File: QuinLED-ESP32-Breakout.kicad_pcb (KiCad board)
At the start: 2 copper layers, 60.8 x 83.7 mm, 22 parts, among them Q1 BC547, U1 QuinLED-ESP32

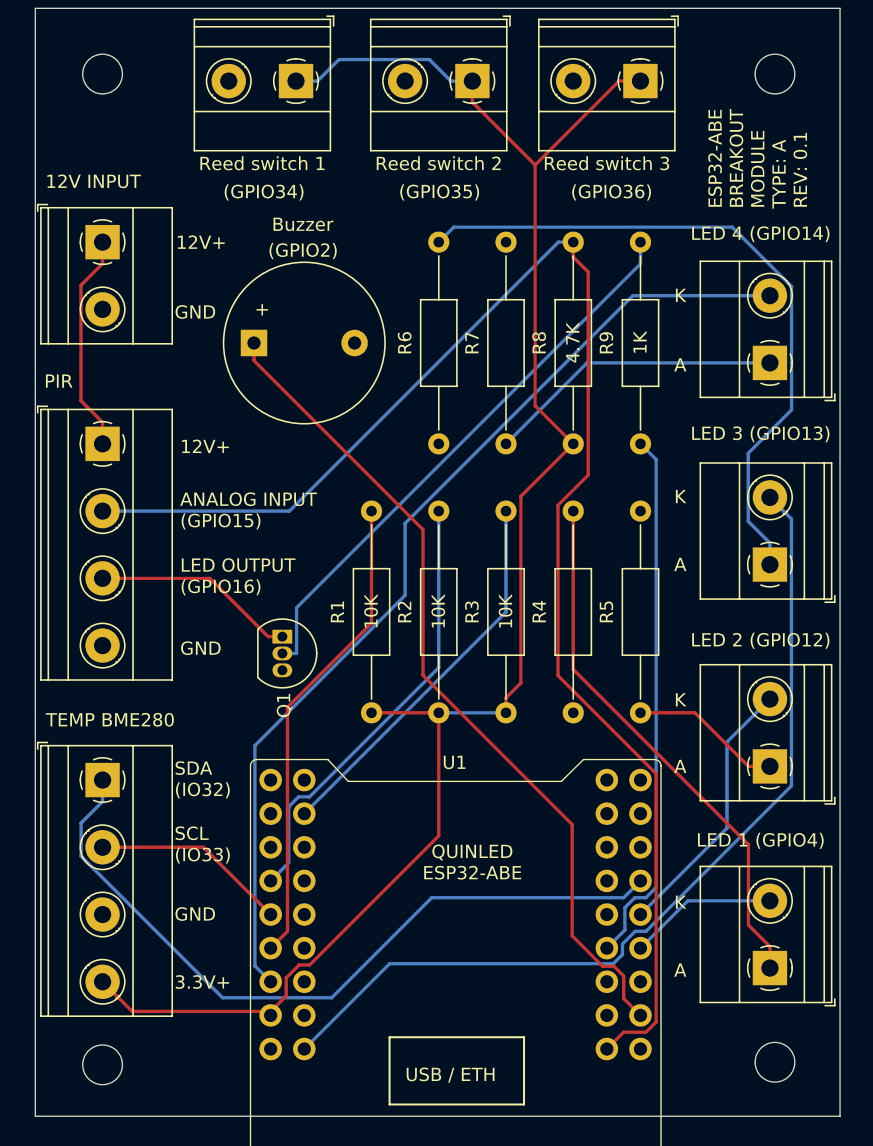
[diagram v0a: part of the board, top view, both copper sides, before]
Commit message: Updated footprint of the buzzer and created all gerber files
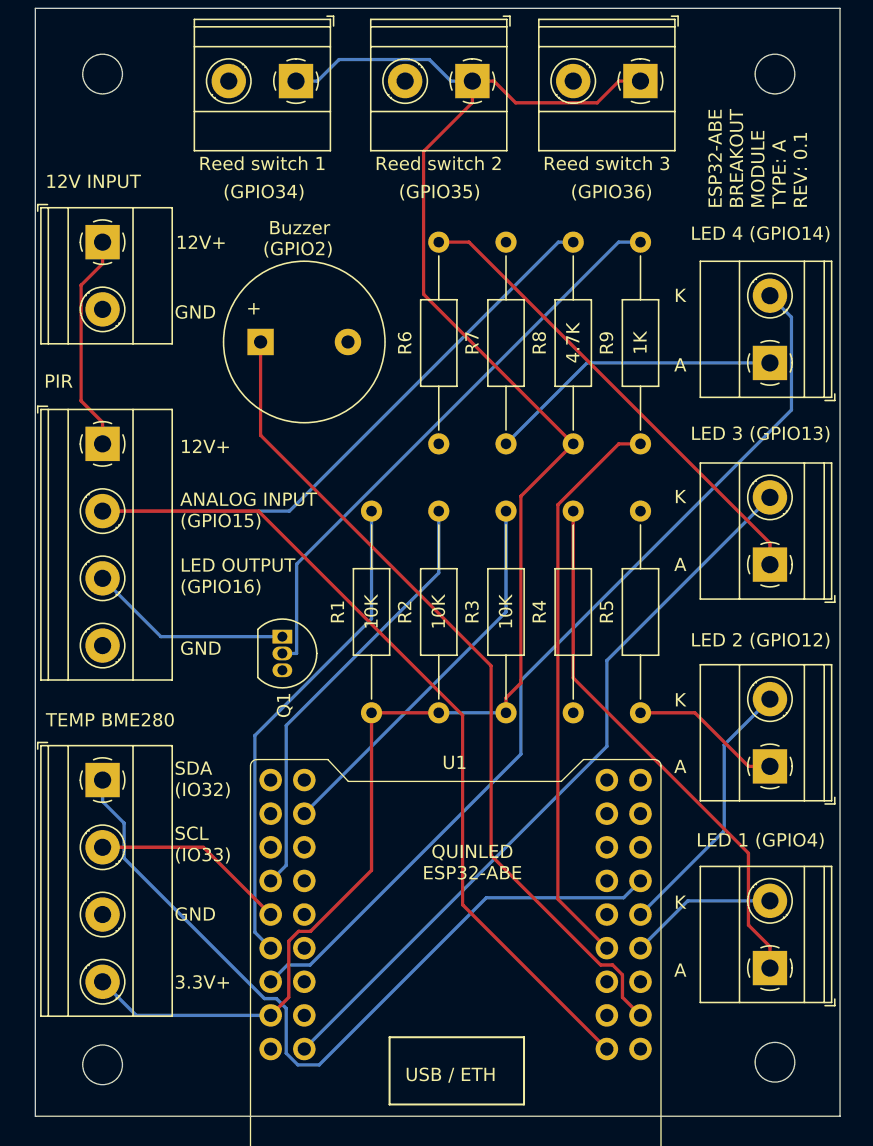
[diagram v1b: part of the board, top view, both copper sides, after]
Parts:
- Buzzer: renamed from Passieve_buzzer1; footprint Buzzer_Beeper:Buzzer_12x9.5RM7.6 -> Custom_footprint_Library:Buzzer_12x9.5RM6.6_custom
- moved Buzzer 3.80 mm to (86.4, 127.0)
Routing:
- net Net-(Led3-Pin_1): track 52.0 -> 36.1 mm
- net GPIO13: track 68.0 -> 56.2 mm
- net GPIO14: track 74.5 -> 69.8 mm
- net GPIO15: track 111.9 -> 107.3 mm
- net +3.3V: track 130.6 -> 135.2 mm
- net GPIO32: track 56.8 -> 59.8 mm
- net GPIO16: track 40.6 -> 43.2 mm
- net GPIO34: track 36.2 -> 37.2 mm
- net Net-(Q1-B): track 42.9 -> 43.9 mm

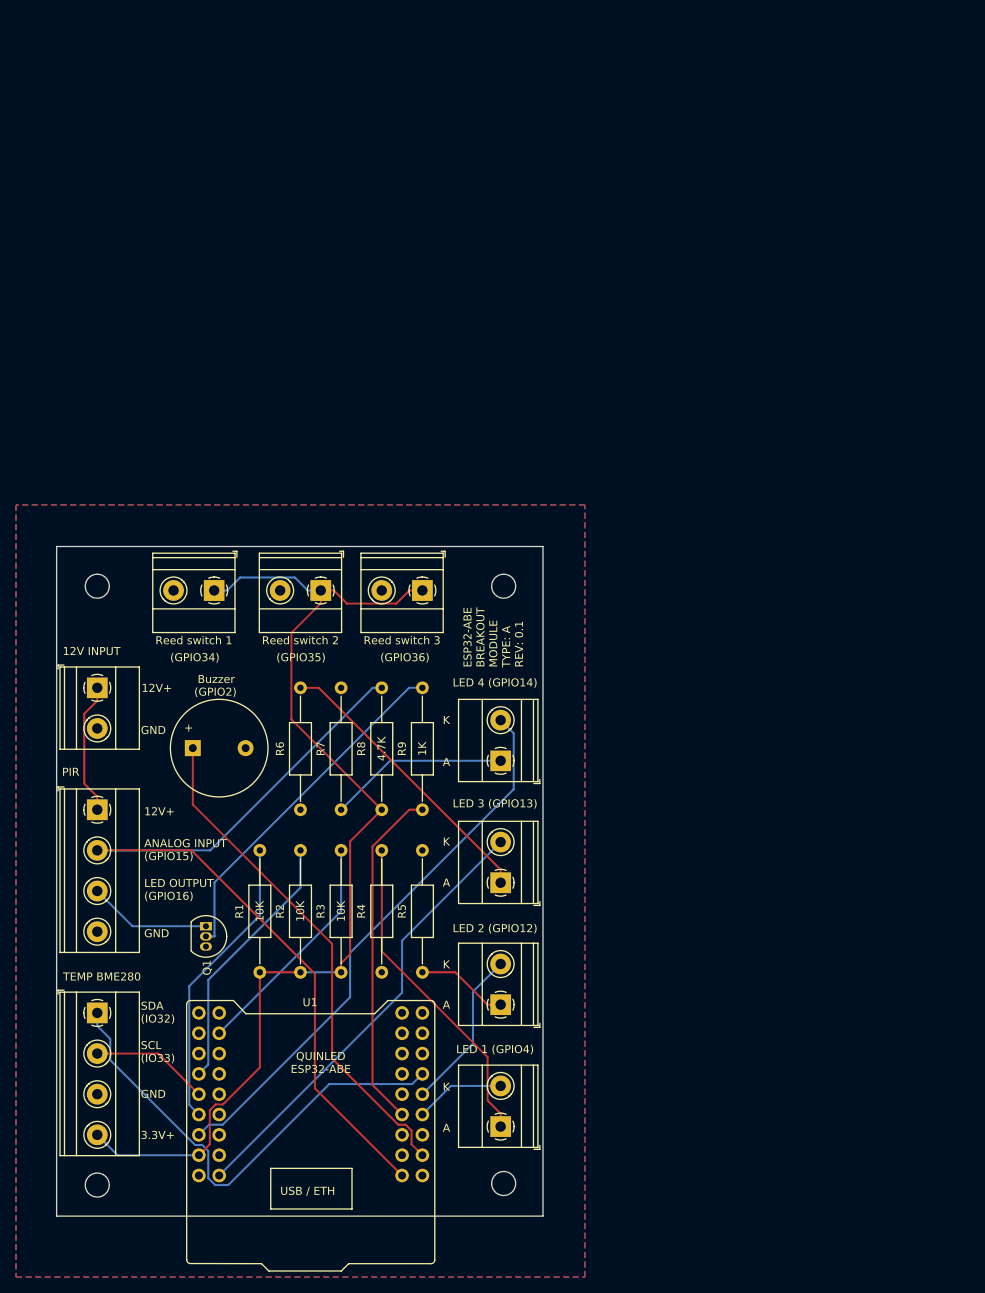
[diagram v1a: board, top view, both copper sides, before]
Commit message: Updatet to new design (rev 0.2)
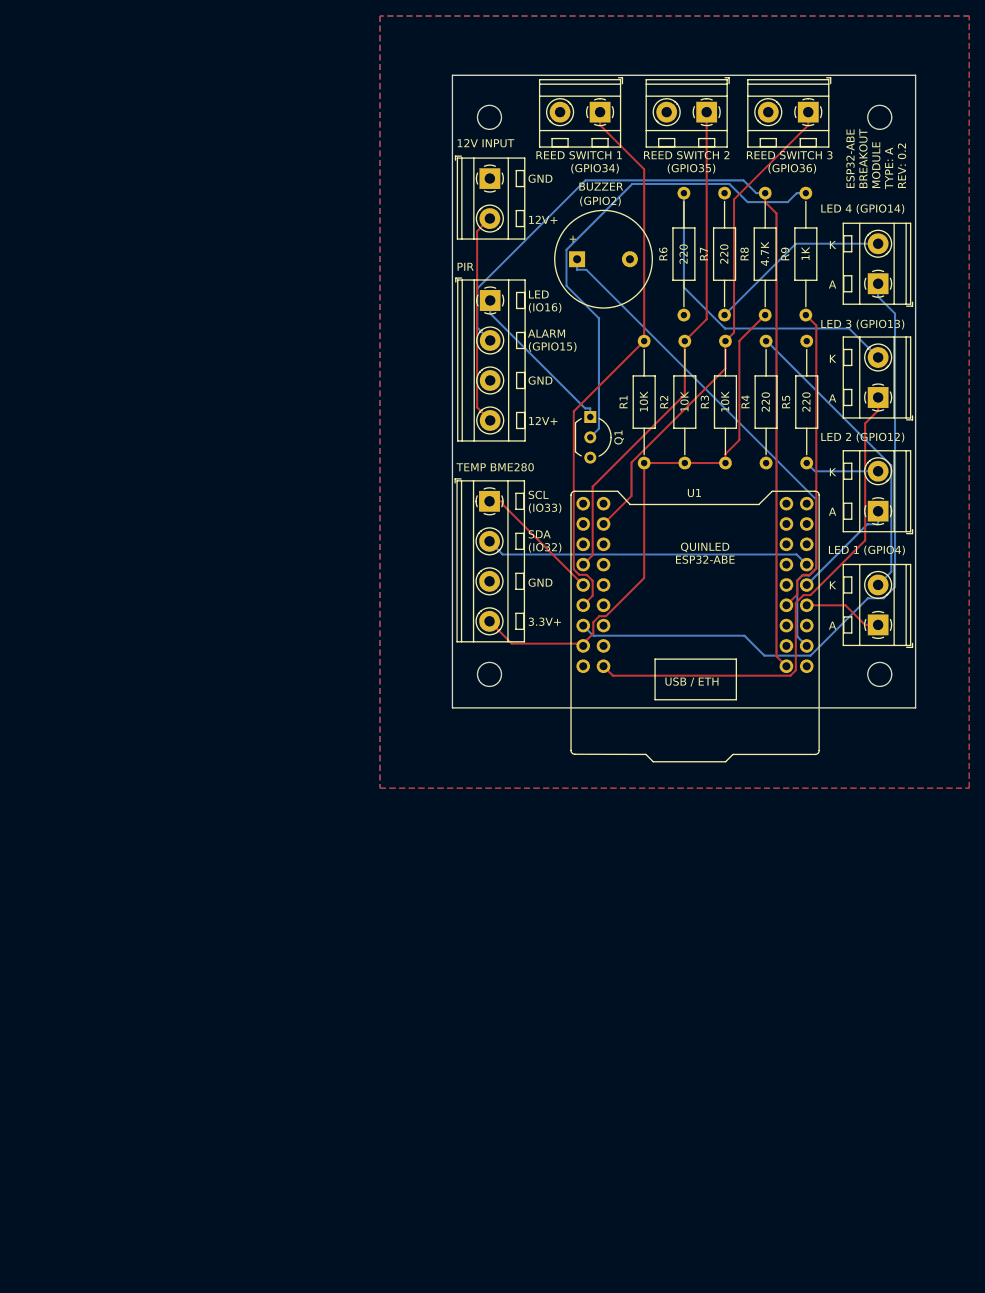
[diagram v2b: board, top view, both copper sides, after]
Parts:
- 12V_voeding_in1: renamed from 12V INPUT; footprint TerminalBlock_Phoenix:TerminalBlock_Phoenix_MKDS-1,5-2-5.08_1x02_P5.08mm_Horizontal -> TerminalBlock_MetzConnect:TerminalBlock_MetzConnect_Type094_RT03502HBLU_1x02_P5.00mm_Horizontal
- Led1: renamed from LED 1 (GPIO4); footprint TerminalBlock_Phoenix:TerminalBlock_Phoenix_MKDS-1,5-2-5.08_1x02_P5.08mm_Horizontal -> TerminalBlock_MetzConnect:TerminalBlock_MetzConnect_Type094_RT03502HBLU_1x02_P5.00mm_Horizontal
- Led2: renamed from LED 2 (GPIO12); footprint TerminalBlock_Phoenix:TerminalBlock_Phoenix_MKDS-1,5-2-5.08_1x02_P5.08mm_Horizontal -> TerminalBlock_MetzConnect:TerminalBlock_MetzConnect_Type094_RT03502HBLU_1x02_P5.00mm_Horizontal
- Led3: renamed from LED 3 (GPIO13); footprint TerminalBlock_Phoenix:TerminalBlock_Phoenix_MKDS-1,5-2-5.08_1x02_P5.08mm_Horizontal -> TerminalBlock_MetzConnect:TerminalBlock_MetzConnect_Type094_RT03502HBLU_1x02_P5.00mm_Horizontal
- Led4: renamed from LED 4 (GPIO14); footprint TerminalBlock_Phoenix:TerminalBlock_Phoenix_MKDS-1,5-2-5.08_1x02_P5.08mm_Horizontal -> TerminalBlock_MetzConnect:TerminalBlock_MetzConnect_Type094_RT03502HBLU_1x02_P5.00mm_Horizontal
- PIR1: renamed from PIR; footprint TerminalBlock_Phoenix:TerminalBlock_Phoenix_MKDS-1,5-4-5.08_1x04_P5.08mm_Horizontal -> TerminalBlock_MetzConnect:TerminalBlock_MetzConnect_Type094_RT03504HBLU_1x04_P5.00mm_Horizontal
- Q1: footprint Package_TO_SOT_THT:TO-92_Inline -> Package_TO_SOT_THT:TO-92_Inline_Wide
- R4, R5, R6, R7: value 10K -> 220
- Reedswitch1: renamed from Reed switch 1; footprint TerminalBlock_Phoenix:TerminalBlock_Phoenix_MKDS-1,5-2-5.08_1x02_P5.08mm_Horizontal -> TerminalBlock_MetzConnect:TerminalBlock_MetzConnect_Type094_RT03502HBLU_1x02_P5.00mm_Horizontal
- Reedswitch2: renamed from Reed switch 2; footprint TerminalBlock_Phoenix:TerminalBlock_Phoenix_MKDS-1,5-2-5.08_1x02_P5.08mm_Horizontal -> TerminalBlock_MetzConnect:TerminalBlock_MetzConnect_Type094_RT03502HBLU_1x02_P5.00mm_Horizontal
- Reedswitch3: renamed from Reed switch 3; footprint TerminalBlock_Phoenix:TerminalBlock_Phoenix_MKDS-1,5-2-5.08_1x02_P5.08mm_Horizontal -> TerminalBlock_MetzConnect:TerminalBlock_MetzConnect_Type094_RT03502HBLU_1x02_P5.00mm_Horizontal
- Temperatuur_BME280: renamed from TEMP BME280; footprint TerminalBlock_Phoenix:TerminalBlock_Phoenix_MKDS-1,5-4-5.08_1x04_P5.08mm_Horizontal -> TerminalBlock_MetzConnect:TerminalBlock_MetzConnect_Type094_RT03504HBLU_1x04_P5.00mm_Horizontal
- moved Temperatuur_BME280 80.6 mm to (120.2, 96.1)
- moved PIR1 80.4 mm to (120.2, 71.0)
- moved 12V_voeding_in1 80.4 mm to (120.2, 55.7)
- moved Q1 79.8 mm to (132.7, 85.5)
- moved R2 79.8 mm to (144.6, 76.0)
- moved R5 79.8 mm to (159.8, 91.3)
- moved U1 79.8 mm to (145.9, 110.9)
- moved R1 79.8 mm to (139.5, 76.0)
- moved R3 79.8 mm to (149.6, 76.0)
- moved R4 79.8 mm to (154.7, 76.0)
- moved Led1 78.5 mm to (168.7, 111.5)
- moved R6 78.2 mm to (144.5, 57.5)
- moved R7 78.2 mm to (149.5, 72.8)
- moved R8 78.2 mm to (154.6, 72.8)
- moved R9 78.2 mm to (159.7, 72.8)
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- renumbered Buzzer to Passieve_buzzer1
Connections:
- 12V_voeding_in1 pad 1: +12V -> GND
- 12V_voeding_in1 pad 2: GND -> +12V
- Led1 pad 1: Net-(Led1-Pin_1) -> GPIO4
- Led1 pad 2: GPIO4 -> Net-(Led1-Pin_2)
- Led2 pad 1: Net-(Led2-Pin_1) -> GPIO12
- Led2 pad 2: GPIO12 -> Net-(Led2-Pin_2)
- Led3 pad 1: Net-(Led3-Pin_1) -> GPIO13
- Led3 pad 2: GPIO13 -> Net-(Led3-Pin_2)
- Led4 pad 1: Net-(Led4-Pin_1) -> GPIO14
- Led4 pad 2: GPIO14 -> Net-(Led4-Pin_2)
- PIR1 pad 1: +12V -> Net-(PIR1-Pin_1)
- PIR1 pad 3: Net-(PIR1-Pin_3) -> GND
- PIR1 pad 4: GND -> +12V
- Q1 pad 1: Net-(PIR1-Pin_3) -> Net-(PIR1-Pin_1)
- R4 pad 1: Net-(Led1-Pin_1) -> Net-(Led1-Pin_2)
- R5 pad 1: Net-(Led2-Pin_1) -> Net-(Led2-Pin_2)
- R6 pad 1: Net-(Led3-Pin_1) -> Net-(Led3-Pin_2)
- R7 pad 1: Net-(Led4-Pin_1) -> Net-(Led4-Pin_2)
- Reedswitch1 pad 1: +3.3V -> GPIO34
- Reedswitch2 pad 1: +3.3V -> GPIO35
- Reedswitch3 pad 1: +3.3V -> GPIO36
- Temperatuur_BME280 pad 1: GPIO32 -> GPIO33
- Temperatuur_BME280 pad 2: GPIO33 -> GPIO32
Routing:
- net +3.3V: track 135.2 -> 70.1 mm
- net Net-(Led1-Pin_1): track 40.7 -> 0.00 mm
- net Net-(Led3-Pin_2): track 0.00 -> 39.7 mm
- net Net-(Led1-Pin_2): track 0.00 -> 37.7 mm
- net Net-(Led3-Pin_1): track 36.1 -> 0.00 mm
- net GPIO36: track 29.2 -> 62.1 mm
- net GPIO34: track 37.2 -> 69.6 mm
- net GPIO35: track 33.2 -> 63.0 mm
- net Net-(Led4-Pin_2): track 0.00 -> 22.9 mm
- net Net-(Led4-Pin_1): track 22.5 -> 0.00 mm
- net Net-(PIR1-Pin_1): track 0.00 -> 20.1 mm
- net GPIO32: track 59.8 -> 40.9 mm
- net Net-(Q1-B): track 43.9 -> 60.3 mm
- net Net-(PIR1-Pin_3): track 15.4 -> 0.00 mm
- net GPIO14: track 69.8 -> 82.9 mm
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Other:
- board size 60.8 x 83.7 mm -> 57.9 x 79.1 mm
- board text added: "12V INPUT"
- board text added: "ALARM (GPIO15)"
- board text added: "BUZZER"
- board text added: "ESP32-ABE BREAKOUT MODULE TYPE: A REV: 0.2"
- board text added: "JLCJLCJLCJLC"
- board text added: "LED (IO16)"
- board text added: "LED 1 (GPIO4)"
- board text added: "LED 2 (GPIO12)"
- board text added: "LED 3 (GPIO13)"
- board text added: "LED 4 (GPIO14)"
- board text added: "LED1: GPIO4 LED2: GPIO12 LED3: GPIO13 LED4: GPIO14 REEDSWITCH SW1: GPIO34 SW2: GPIO35 SW3: GPIO36 PIR: LED: GPIO16 ALARM: GPIO15"
- board text added: "PIR"
- board text added: "REED SWITCH 1"
- board text added: "REED SWITCH 2"
- board text added: "REED SWITCH 3"
- board text added: "TEMP BME280"
- board text added: "TEMP: SDA: GPIO32 SCL: GPIO33 BUZZER: GPIO2"
- board text removed: "ANALOG INPUT (GPIO15)"
- board text removed: "ESP32-ABE BREAKOUT MODULE TYPE: A REV: 0.1"
- board text removed: "LED OUTPUT (GPIO16)"
